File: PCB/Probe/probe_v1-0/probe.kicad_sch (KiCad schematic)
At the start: 0 parts

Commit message: Probe-Schematic editing
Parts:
- added C1, C3, C8: 0.1uF, symbol Device:C
- added C10, C2, C4, C7, C9: 22uF, symbol Device:C_Polarized_US
- added C11, C12: C, symbol Device:C
- added C5: 0.33uF, symbol Device:C
- added C6: 100uF, symbol Device:C_Polarized_US
- added D1, D2: D_Schottky, symbol Device:D_Schottky
- added D3: RED, symbol Device:LED
- added D4: BLUE, symbol Device:LED
- added D5: LED, symbol Device:LED
- added J1: Conn_01x02, symbol Connector_Generic:Conn_01x02
- added J2: USB_B_Micro, symbol Connector:USB_B_Micro
- added J3: Conn_01x06, symbol Connector_Generic:Conn_01x06
- added R1, R2: 470, symbol Device:R
- added R3, R4, R5, R6, R7: 10K, symbol Device:R
- added SW1, SW2: SW_Push, symbol Switch:SW_Push
- added U2: AMS1117-3.3, Package_TO_SOT_SMD:SOT-223-3_TabPin2, symbol Regulator_Linear:AMS1117-3.3
- added U3: AMS1117-5.0, Package_TO_SOT_SMD:SOT-223-3_TabPin2, symbol Regulator_Linear:AMS1117-5.0
- added U4: ESP32-S2-MINI-1, PCM_Espressif:ESP32-S2-MINI-1, symbol PCM_Espressif:ESP32-S2-MINI-1
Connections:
- new net: C12.2, R2.1, SW2.2
- new net: D5.2 (A), R5.1
- new net: D4.2 (A), R4.1
- new net: C7.1, C8.1, D2.2 (A), U3.2 (VO)
- new net: D3.2 (A), R3.1
- new net: C11.1, R1.1, SW1.2
- new net: D1.2 (A), J2.1 (VBUS)
- new net 3V3: C10.1, C2.1, C3.1, J3.5 (Pin_5), R5.2, R6.2, R7.2, U2.2 (VO), U4.3 (3V3)
- new net 5V: C1.1, C4.1, C9.1, D1.1 (K), D2.1 (K), J3.6 (Pin_6), R4.2, U2.3 (VI)
- new net 9V: C5.1, C6.1, J1.2 (Pin_2), R3.2, U3.3 (VI)
- new net D+: J2.3 (D+), U4.24 (USB_D+/ADC2_CH9/GPIO20)
- new net D-: J2.2 (D-), U4.23 (USB_D-/ADC2_CH8/GPIO19)
- new net EN: R1.2, R7.1, U4.45 (CHIP/PU/RESET)
- new net GND: C1.2, C10.2, C11.2, C12.1, C2.2, C3.2, C4.2, C5.2, C6.2, C7.2, C8.2, C9.2, D3.1 (K), D4.1 (K), D5.1 (K), J1.1 (Pin_1), J2.4 (ID), J2.5 (GND), J2.6 (Shield), J3.1 (Pin_1), SW1.1, SW2.1, U2.1 (GND), U3.1 (GND), U4.1 (GND), U4.2 (GND), U4.30 (GND), U4.42 (GND), U4.43 (GND), U4.46 (GND), U4.47 (GND), U4.48 (GND), U4.49 (GND), U4.50 (GND), U4.51 (GND), U4.52 (GND), U4.53 (GND), U4.54 (GND), U4.55 (GND), U4.56 (GND), U4.57 (GND), U4.58 (GND), U4.59 (GND), U4.60 (GND), U4.61 (GND), U4.62 (GND), U4.63 (GND), U4.64 (GND), U4.65 (GND)
- new net GPIO0: R2.2, R6.1, U4.4 (GPIO0/BOOT)
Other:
- note added: "3V3 Reg"
- note added: "5V Reg"
- note added: "BOOT"
- note added: "EN"
- note added: "Electrolytic Discharge Capacitors"
- note added: "Indicator LEDs"
- note added: "POWER"
- note added: "Power From Supply"
- note added: "Push Buttons"
- note added: "Test Points"
- note added: "USB-Micro PWR & PGR"

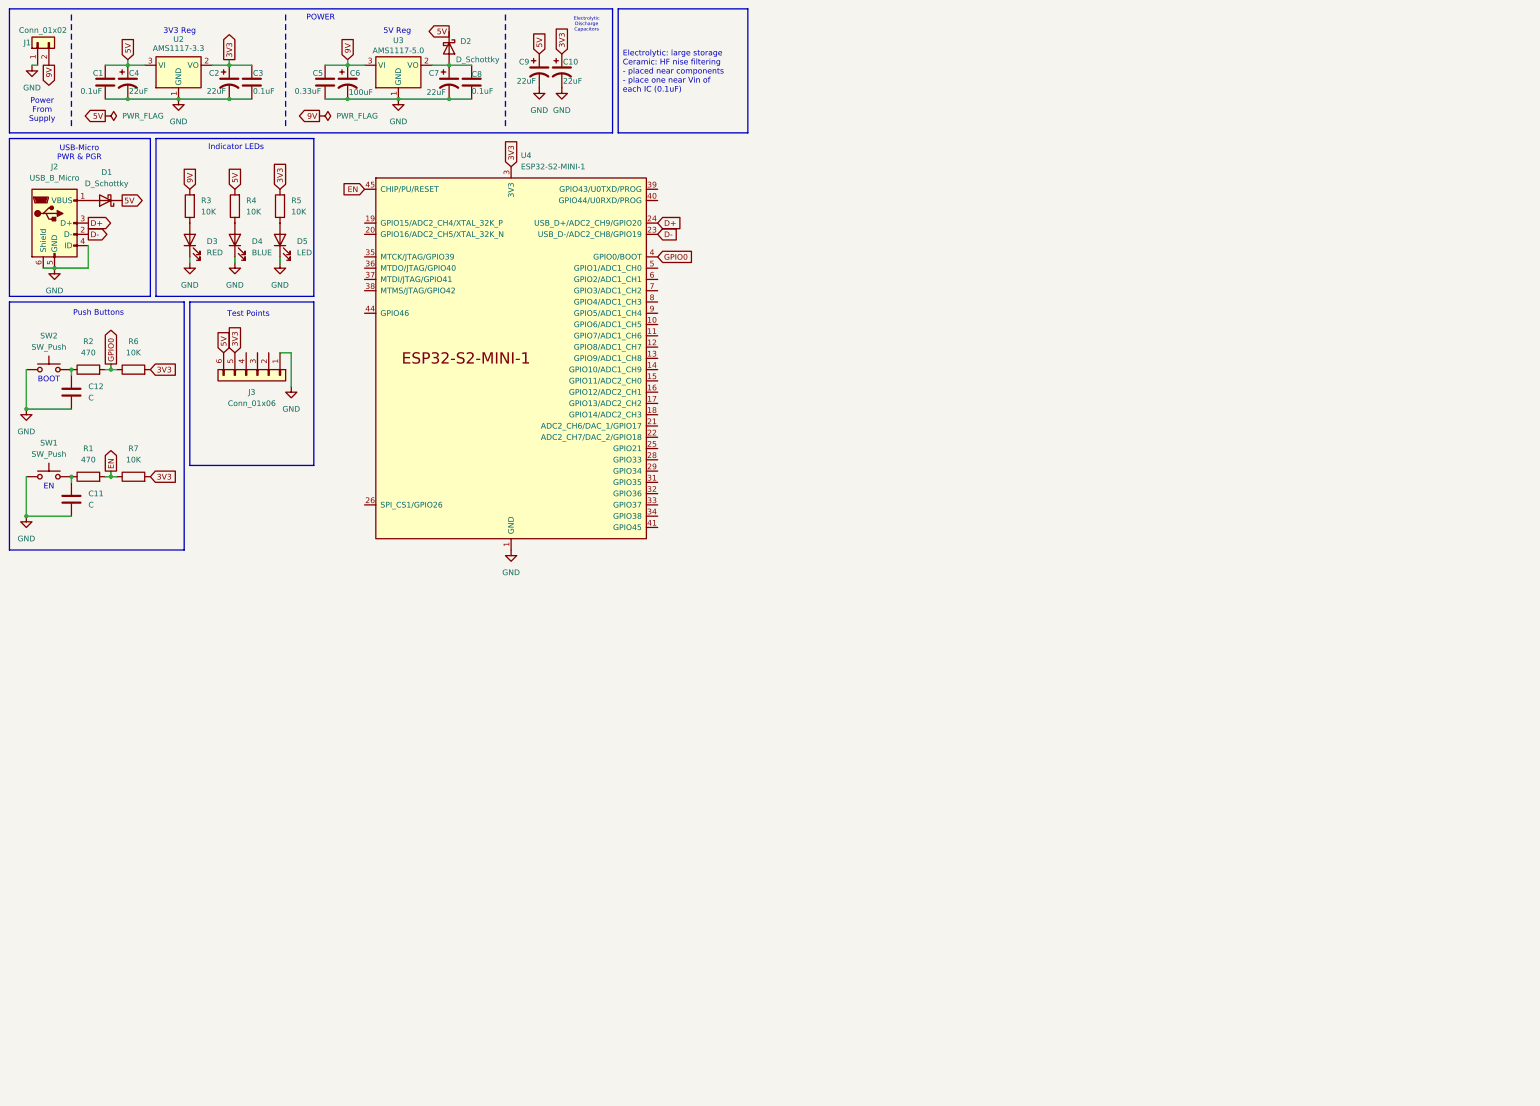
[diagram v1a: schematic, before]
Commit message: Updated PCB
Added Measuring Circuitry
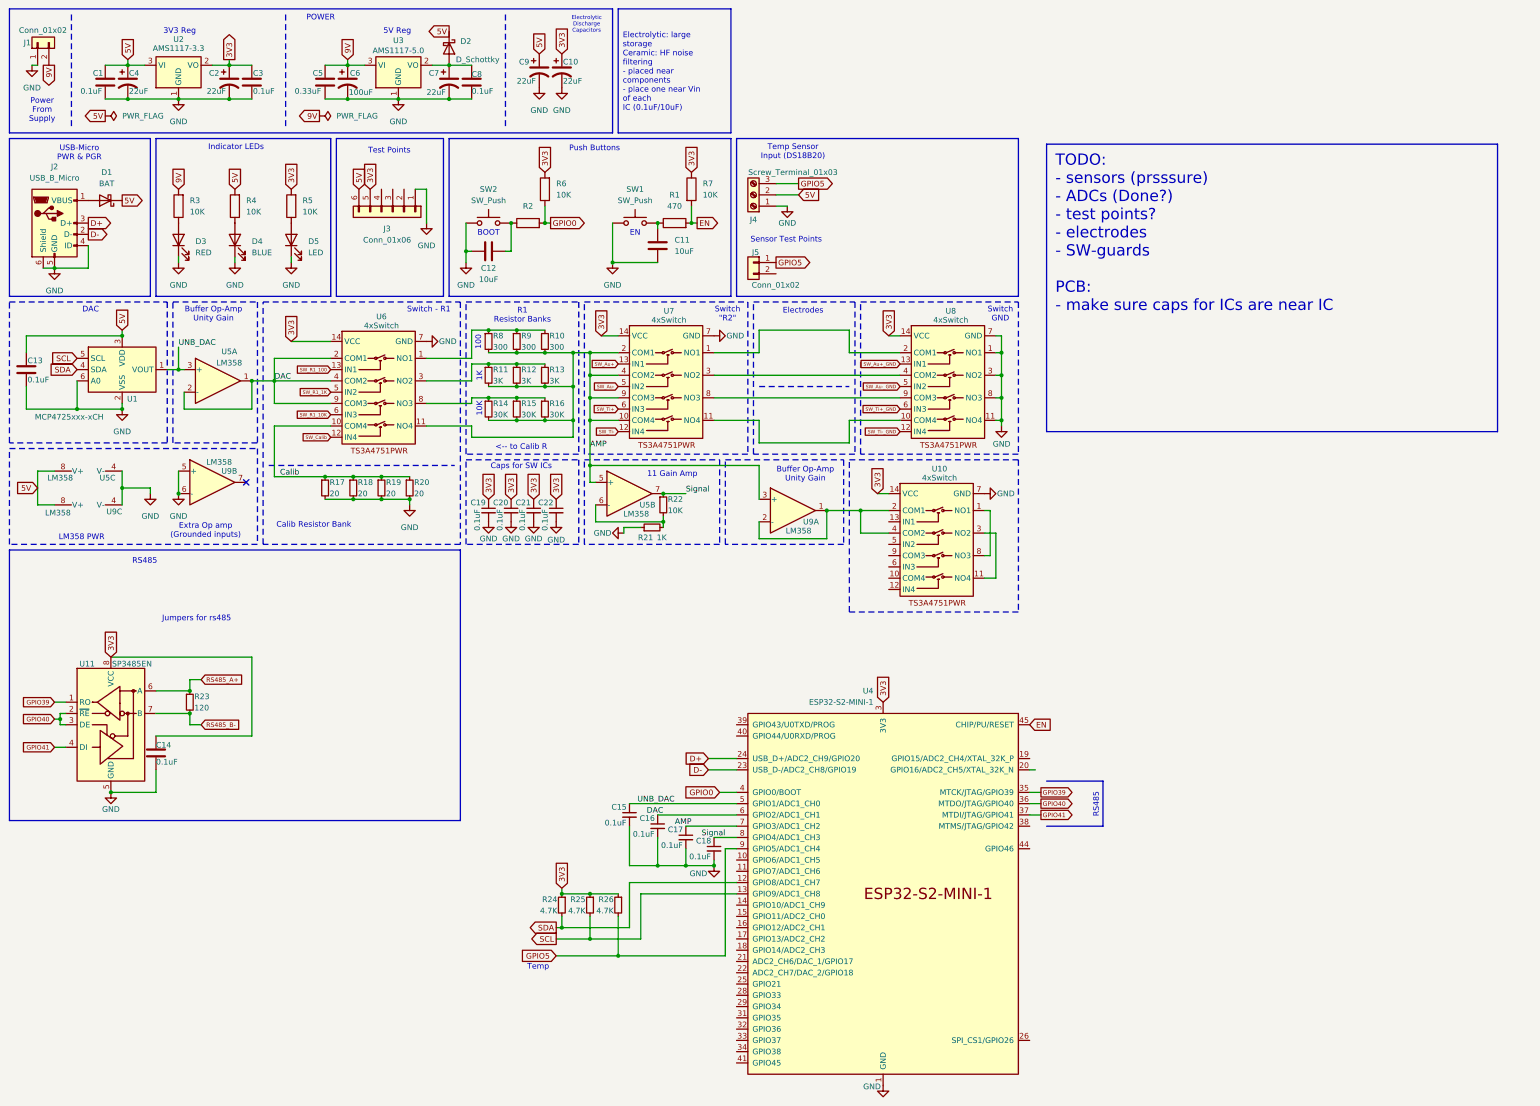
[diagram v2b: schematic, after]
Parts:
- added C13, C14: 0.1uF, symbol Device:C
- added C15, C16, C17, C18, C19, C20, C21, C22: 0.1uF, symbol Device:C_Small
- added J4: Screw_Terminal_01x03, symbol Connector:Screw_Terminal_01x03
- added J5: Conn_01x02, symbol Connector_Generic:Conn_01x02
- added R10, R8, R9: 300, symbol Device:R_Small
- added R11, R12, R13: 3K, symbol Device:R_Small
- added R14, R15, R16: 30K, symbol Device:R_Small
- added R17, R18, R19, R20: 20, symbol Device:R_Small
- added R21: 1K, symbol Device:R_Small
- added R22: 10K, symbol Device:R_Small
- added R23: 120, symbol Device:R_Small
- added R24, R25, R26: 4.7K, symbol Device:R_Small
- added U1: MCP4725xxx-xCH, Package_TO_SOT_SMD:SOT-23-6, symbol Analog_DAC:MCP4725xxx-xCH
- added U10, U6, U7, U8: 4xSwitch, Package_SO:TSSOP-14_4.4x5mm_P0.65mm, symbol ThesisLibrary:TS3A4751PWR
- added U11: SP3485EN, Package_SO:SOIC-8_3.9x4.9mm_P1.27mm, symbol Interface_UART:SP3485EN
- added U5, U9: LM358, symbol Amplifier_Operational:LM358
- C11, C12: value C -> 10uF
- D1: value D_Schottky -> BAT
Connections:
- net 3V3: now also R7.1, C14.1, C19.1, C20.1, C21.1, C22.1, R24.1, R25.1, R26.1, U10.14 (VCC), U11.8 (VCC), U6.14 (VCC), U7.14 (VCC), U8.14 (VCC); no longer R7.2
- net 5V: now also C13.1, J4.2 (Pin_2), U1.3 (VDD), U5.8 (V+), U9.8 (V+)
- net EN: now also R7.2; no longer R7.1
- net GND: now also C12.2, C13.2, C14.2, C15.2, C16.2, C17.2, C18.2, C19.2, C20.2, C21.2, C22.2, J4.1 (Pin_1), R17.2, R18.2, R19.2, R20.2, R21.1, U1.2 (VSS), U1.6 (A0), U10.7 (GND), U11.5 (GND), U5.4 (V-), U6.7 (GND), U7.7 (GND), U8.1 (NO1), U8.11 (NO4), U8.3 (NO2), U8.7 (GND), U8.8 (NO3), U9.4 (V-), U9.5 (+), U9.6 (-); no longer C12.1
- net at R2.1, SW2.2: now also C12.1; no longer C12.2
- net SDA: now reaches U4.12 (GPIO8/ADC1_CH7)
- net SDA: now also R24.2, U1.4 (SDA)
- net SCL: now reaches U4.13 (GPIO9/ADC1_CH8)
- net SCL: now also R25.2, U1.5 (SCL)
- net GPIO39: now reaches U4.35 (MTCK/JTAG/GPIO39)
- net GPIO39: now also U11.1 (RO)
- net GPIO40: now reaches U4.36 (MTDO/JTAG/GPIO40)
- net GPIO40: now also U11.2 (~{RE}), U11.3 (DE)
- net GPIO41: now reaches U4.37 (MTDI/JTAG/GPIO41)
- net GPIO41: now also U11.4 (DI)
- net UNB_DAC: now reaches U4.5 (GPIO1/ADC1_CH0)
- net UNB_DAC: now also C15.1, U1.1 (VOUT), U5.3 (+)
- net DAC: now reaches U4.6 (GPIO2/ADC1_CH1)
- net DAC: now also C16.1, U5.1, U5.2 (-), U6.2 (COM1), U6.4 (COM2), U6.9 (COM3)
- net AMP: now reaches U4.7 (GPIO3/ADC1_CH2)
- net AMP: now also C17.1, R10.2, R11.2, R12.2, R13.2, R14.2, R15.2, R16.2, R8.2, R9.2, U5.5 (+), U6.11 (NO4), U7.10 (COM4), U7.2 (COM1), U7.4 (COM2), U7.9 (COM3), U9.3 (+)
- net Signal: now reaches U4.8 (GPIO4/ADC1_CH3)
- net Signal: now also C18.1, R22.1, U5.7
- net GPIO5: now reaches U4.9 (GPIO5/ADC1_CH4)
- net GPIO5: now also J4.3 (Pin_3), J5.1 (Pin_1), R26.2
- new net: R14.1, R15.1, R16.1, U6.8 (NO3)
- new net: R10.1, R8.1, R9.1, U6.1 (NO1)
- new net: R21.2, R22.2, U5.6 (-)
- new net: U10.1 (NO1), U10.8 (NO3)
- new net: U10.11 (NO4), U10.3 (NO2)
- new net: U10.2 (COM1), U10.4 (COM2), U9.1, U9.2 (-)
- new net: R11.1, R12.1, R13.1, U6.3 (NO2)
- new net: U7.11 (NO4), U8.10 (COM4)
- new net: U7.1 (NO1), U8.2 (COM1)
- new net: U7.3 (NO2), U8.4 (COM2)
- new net: U7.8 (NO3), U8.9 (COM3)
- new net Calib: R17.1, R18.1, R19.1, R20.1, U6.10 (COM4)
- new net RS485_A+: R23.1, U11.6 (A)
- new net RS485_B-: R23.2, U11.7 (B)
- new net SW_Au+: U7.13 (IN1)
- new net SW_Au+_GND: U8.13 (IN1)
- new net SW_Au-: U7.5 (IN2)
- new net SW_Au-_GND: U8.5 (IN2)
- new net SW_Calib: U6.12 (IN4)
- new net SW_R1_100: U6.13 (IN1)
- new net SW_R1_10K: U6.6 (IN3)
- new net SW_R1_1K: U6.5 (IN2)
- new net SW_Ti+: U7.6 (IN3)
- new net SW_Ti+_GND: U8.6 (IN3)
- new net SW_Ti-: U7.12 (IN4)
- new net SW_Ti-_GND: U8.12 (IN4)
- no-connect marks 0 -> 1
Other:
- note added: "100"
- note added: "10K"
- note added: "11 Gain Amp"
- note added: "1K"
- note added: "<-- to Calib R"
- note added: "Buffer Op-Amp Unity Gain"
- note added: "Calib Resistor Bank"
- note added: "Caps for SW ICs"
- note added: "DAC"
- note added: "Electrodes"
- note added: "Extra Op amp (Grounded inputs)"
- note added: "Jumpers for rs485"
- note added: "LM358 PWR"
- note added: "R1 Resistor Banks"
- note added: "RS485"
- note added: "Sensor Test Points"
- note added: "Switch "R2""
- note added: "Switch - R1"
- note added: "Switch GND"
- note added: "Temp"
- note added: "Temp Sensor Input (DS18B20)"
- moved on the sheet: C11, C12, D3, D5, J3, R1, R2, R3, R5, R6, R7, SW1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

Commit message: small probe pcb updates
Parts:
- added J6: Conn_01x04_Socket, symbol Connector:Conn_01x04_Socket
- added R27, R28: 4.7K, symbol Device:R_Small
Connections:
- net 3V3: now also R27.1
- net 5V: now also J6.4 (Pin_4)
- net AMP: now also J3.2 (Pin_2)
- net DAC: now also J3.3 (Pin_3)
- net GND: now also J6.1 (Pin_1), R28.2; no longer J3.1 (Pin_1)
- net RS485_A+: now also J6.3 (Pin_3), R27.2
- net RS485_B-: now also J6.2 (Pin_2), R28.1
- net Signal: now also J3.1 (Pin_1)
- net UNB_DAC: now also J3.4 (Pin_4)
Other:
- note added: "- Jumpers for rs485 - check connection in datasheet"
- note added: "Calibration Resistor Bank"
- note added: "SW - Au Guard"
- note removed: "Calib Resistor Bank"
- note removed: "Jumpers for rs485"
- moved on the sheet: J3, R17, R18, R19, R20, R23, R24, R25, R26, U11, U5A, U5C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
